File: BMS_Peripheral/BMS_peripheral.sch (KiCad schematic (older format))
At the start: 187 parts, among them J1 isoSPI-Cutout, J2 isoSPI-Cutout, J3 MM_F_VT_16, J4 MM_F_VT_20, Q10 BSS308PE, Q11 NSS1C201MZ4, Q2 BSS308PE, Q3 BSS308PE, Q4 BSS308PE, Q5 BSS308PE, Q7 BSS308PE, Q8 BSS308PE, Q9 BSS308PE, T1 T_LAN_7490100111A, U1 LTC6811-1, U2 24AA01, U3 MCP6001T-I-LT, U4 MCP6001T-I-LT, U5 LTC1380IGN, U6 LTC1380IGN, U7 LTC1380IGN

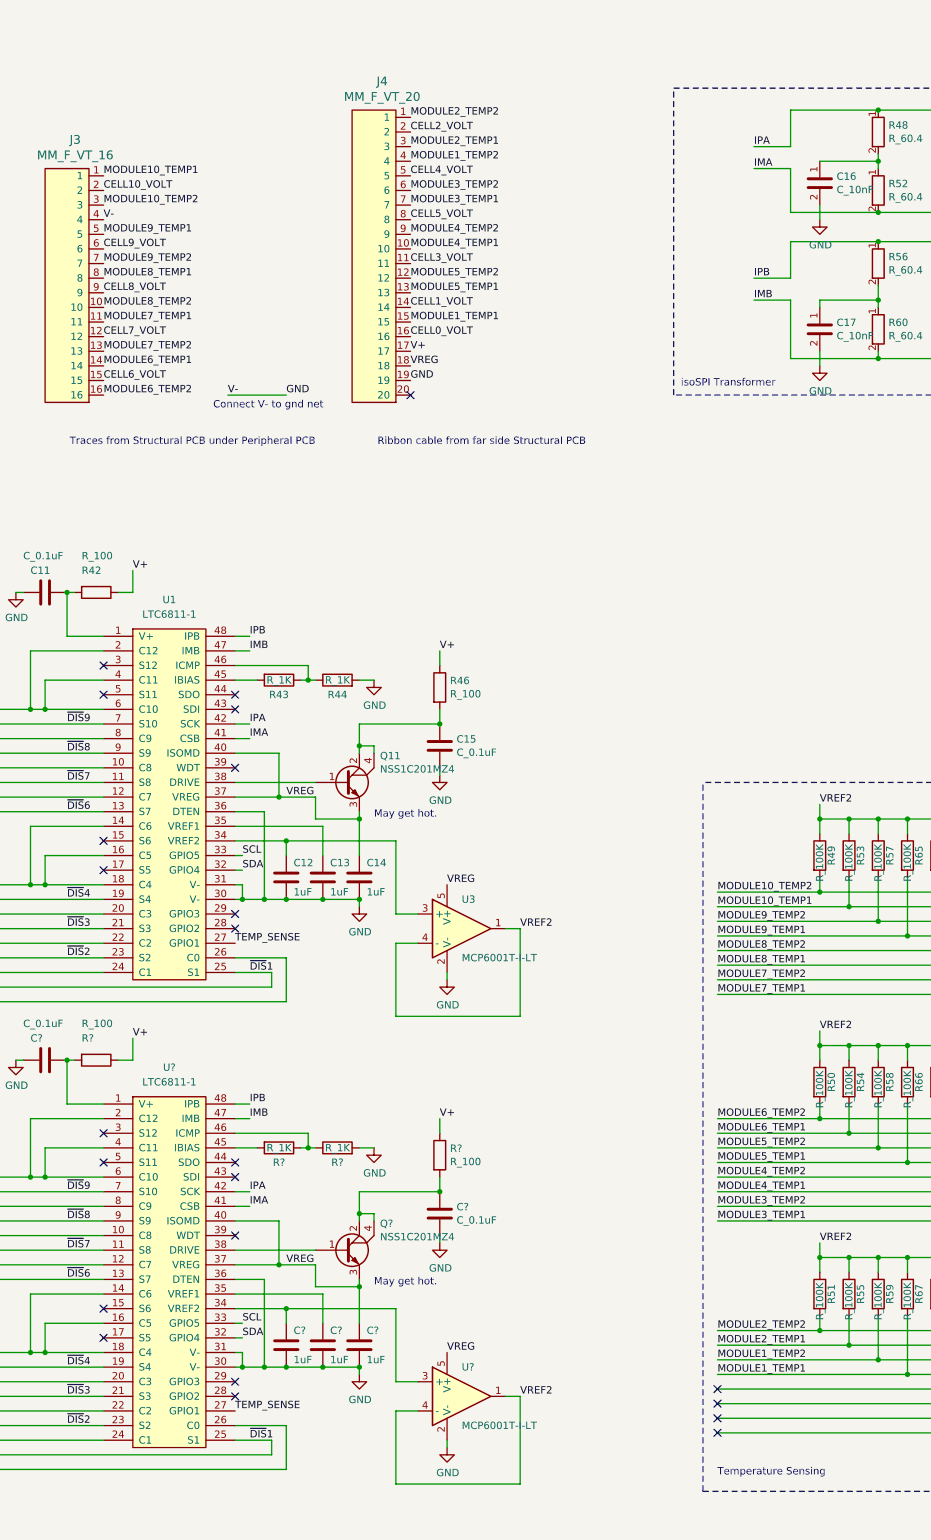
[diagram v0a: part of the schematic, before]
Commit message: Updated muxes for temp sensing
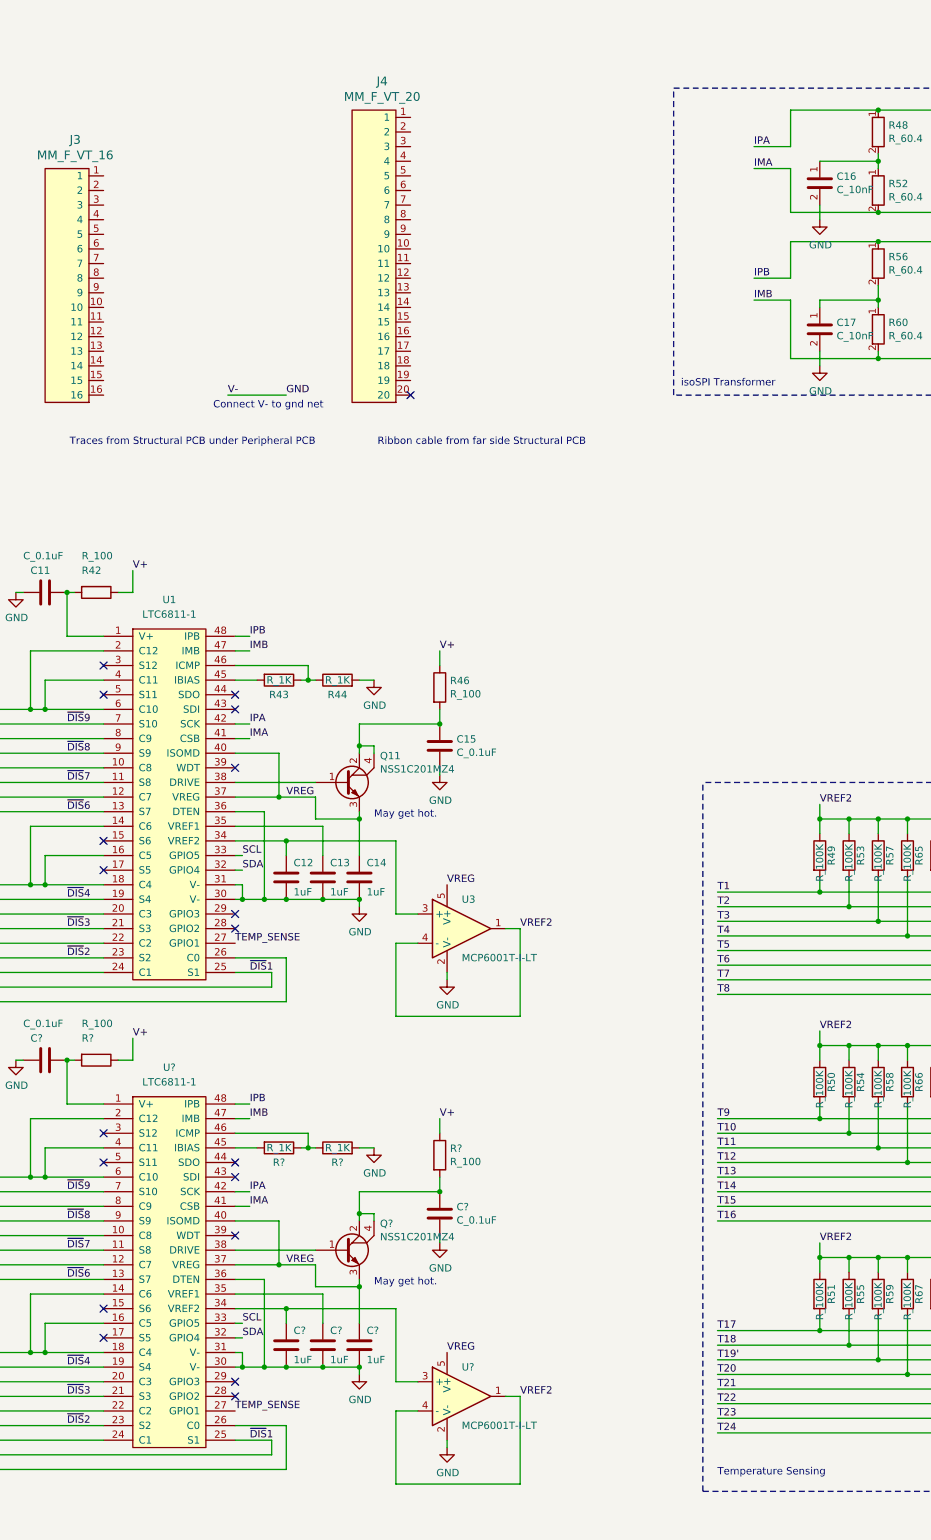
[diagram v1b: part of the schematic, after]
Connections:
- net CELL0_VOLT: no longer J4.16
- net CELL10_VOLT: no longer J3.2
- net CELL1_VOLT: no longer J4.14
- net CELL2_VOLT: no longer J4.2
- net CELL4_VOLT: no longer J4.5
- net CELL5_VOLT: no longer J4.8
- net CELL7_VOLT: no longer J3.12
- net CELL8_VOLT: no longer J3.9
- net CELL9_VOLT: no longer J3.6
- net GND: no longer J3.4, J4.19
- net V+: no longer J4.17
- net VREG: no longer J4.18
- net T21: now reaches R71.2, U7.5 (S4)
- net T22: now reaches R75.2, U7.6 (S5)
- net T23: now reaches R78.2, U7.7 (S6)
- net T24: now reaches R81.2, U7.8 (S7)
- net CELL3_VOLT: no longer names the net of J4.11
- net CELL6_VOLT: no longer names the net of J3.15
- net MODULE10_TEMP1 renamed T2
- net T2: no longer J3.1
- net MODULE10_TEMP2 renamed T1
- net T1: no longer J3.3
- net MODULE1_TEMP1 renamed T20
- net T20: no longer J4.15
- net MODULE1_TEMP2 renamed T19'
- net T19': no longer J4.4
- net MODULE2_TEMP1 renamed T18
- net T18: no longer J4.3
- net MODULE2_TEMP2 renamed T17
- net T17: no longer J4.1
- net MODULE3_TEMP1 renamed T16
- net T16: no longer J4.7
- net MODULE3_TEMP2 renamed T15
- net T15: no longer J4.6
- net MODULE4_TEMP1 renamed T14
- net T14: no longer J4.10
- net MODULE4_TEMP2 renamed T13
- net T13: no longer J4.9
- net MODULE5_TEMP1 renamed T12
- net T12: no longer J4.13
- net MODULE5_TEMP2 renamed T11
- net T11: no longer J4.12
- net MODULE6_TEMP1 renamed T10
- net T10: no longer J3.14
- net MODULE6_TEMP2 renamed T9
- net T9: no longer J3.16
- net MODULE7_TEMP1 renamed T8
- net T8: no longer J3.11
- net MODULE7_TEMP2 renamed T7
- net T7: no longer J3.13
- net MODULE8_TEMP1 renamed T6
- net T6: no longer J3.8
- net MODULE8_TEMP2 renamed T5
- net T5: no longer J3.10
- net MODULE9_TEMP1 renamed T4
- net T4: no longer J3.5
- net MODULE9_TEMP2 renamed T3
- net T3: no longer J3.7
- no-connect marks 41 -> 37
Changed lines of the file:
@@
 	11550 7500 13650 7500
 Text Label 11550 6900 0    50   ~ 0
-MODULE10_TEMP1
+T2
 Text Label 11550 7000 0    50   ~ 0
-MODULE9_TEMP2
+T3
 Text Label 11550 7100 0    50   ~ 0
-MODULE9_TEMP1
+T4
 Text Label 11550 7200 0    50   ~ 0
-MODULE8_TEMP2
+T5
 Text Label 11550 7300 0    50   ~ 0
-MODULE8_TEMP1
+T6
 Text Label 11550 7400 0    50   ~ 0
-MODULE7_TEMP2
+T7
 Text Label 11550 7500 0    50   ~ 0
-MODULE7_TEMP1
+T8
 Wire Wire Line
 	12250 6700 12250 6800
@@
 	11550 9050 13650 9050
 Text Label 11550 8450 0    50   ~ 0
-MODULE6_TEMP1
+T10
 Text Label 11550 8550 0    50   ~ 0
-MODULE5_TEMP2
+T11
 Text Label 11550 8650 0    50   ~ 0
-MODULE5_TEMP1
+T12
 Text Label 11550 8850 0    50   ~ 0
-MODULE4_TEMP1
+T14
 Text Label 11550 8950 0    50   ~ 0
-MODULE3_TEMP2
+T15
 Text Label 11550 9050 0    50   ~ 0
-MODULE3_TEMP1
+T16
 Wire Wire Line
 	12250 8250 12250 8350
@@
 	11550 10500 13650 10500
 Text Label 11550 9800 0    50   ~ 0
-MODULE2_TEMP2
+T17
 Text Label 11550 9900 0    50   ~ 0
-MODULE2_TEMP1
+T18
 Text Label 11550 10000 0    50   ~ 0
-MODULE1_TEMP2
+T19'
 Text Label 11550 10100 0    50   ~ 0
-MODULE1_TEMP1
+T20
 Wire Wire Line
 	12250 9700 12250 9800
@@
 A0 = 0, A1 = 0  Address 0x94
 Text Label 11550 6800 0    50   ~ 0
-MODULE10_TEMP2
+T1
 Text Label 11550 8350 0    50   ~ 0
-MODULE6_TEMP2
+T9
 Text Label 11550 8750 0    50   ~ 0
-MODULE4_TEMP2
+T13
 Wire Wire Line
 	15050 10100 15050 10300
@@
 Wire Wire Line
 	8800 6050 8250 6050
-Text Label 7350 2000 0    50   ~ 0
-CELL10_VOLT
-Text Label 7350 2400 0    50   ~ 0
-CELL9_VOLT
-Text Label 7350 2700 0    50   ~ 0
-CELL8_VOLT
-Text Label 7350 3000 0    50   ~ 0
-CELL7_VOLT
-Text Label 7350 3300 0    50   ~ 0
-CELL6_VOLT
 Wire Notes Line
 	11450 10900 17550 10900
-NoConn ~ 11550 10300
-NoConn ~ 11550 10400
-NoConn ~ 11550 10500
 Wire Notes Line
 	17550 6050 17550 10900
@@
 	1    0    0    -1
 $EndComp
-Text Label 7350 1900 0    50   ~ 0
-MODULE10_TEMP1
-Text Label 7350 2100 0    50   ~ 0
-MODULE10_TEMP2
-Text Label 7350 2300 0    50   ~ 0
-MODULE9_TEMP1
-Text Label 7350 2500 0    50   ~ 0
-MODULE9_TEMP2
-Text Label 7350 2600 0    50   ~ 0
-MODULE8_TEMP1
-Text Label 7350 2800 0    50   ~ 0
-MODULE8_TEMP2
-Text Label 7350 2900 0    50   ~ 0
-MODULE7_TEMP1
-Text Label 7350 3100 0    50   ~ 0
-MODULE7_TEMP2
-Text Label 7350 3200 0    50   ~ 0
-MODULE6_TEMP1
-Text Label 7350 3400 0    50   ~ 0
-MODULE6_TEMP2
-Text Label 7350 2200 0    50   ~ 0
-V-
-Text Label 9450 2200 0    50   ~ 0
-CELL5_VOLT
-Text Label 9450 1900 0    50   ~ 0
-CELL4_VOLT
-Text Label 9450 2500 0    50   ~ 0
-CELL3_VOLT
-Text Label 9450 1600 0    50   ~ 0
-CELL2_VOLT
-Text Label 9450 2700 0    50   ~ 0
-MODULE5_TEMP1
-Text Label 9450 2600 0    50   ~ 0
-MODULE5_TEMP2
-Text Label 9450 2400 0    50   ~ 0
-MODULE4_TEMP1
-Text Label 9450 2300 0    50   ~ 0
-MODULE4_TEMP2
-Text Label 9450 2100 0    50   ~ 0
-MODULE3_TEMP1
-Text Label 9450 2000 0    50   ~ 0
-MODULE3_TEMP2
-Text Label 9450 1700 0    50   ~ 0
-MODULE2_TEMP1
-Text Label 9450 1500 0    50   ~ 0
-MODULE2_TEMP2
-Text Label 9450 2900 0    50   ~ 0
-MODULE1_TEMP1
-Text Label 9450 1800 0    50   ~ 0
-MODULE1_TEMP2
-Text Label 9450 3100 0    50   ~ 0
-V+
-Text Label 9450 2800 0    50   ~ 0
-CELL1_VOLT
-Text Label 9450 3000 0    50   ~ 0
-CELL0_VOLT
 Text Label 1750 750  2    50   ~ 0
 CELL16_VOLT
@@
 	1    0    0    -1
 $EndComp
-Text Label 9450 3300 0    50   ~ 0
-GND
 NoConn ~ 9450 3400
 Wire Wire Line
@@
 Wire Wire Line
 	1750 7550 2600 7550
-NoConn ~ 11550 10200
-Text Label 9450 3200 0    50   ~ 0
-VREG
 $Comp
 L formula:T_LAN_7490100111A T1
@@
 Wire Wire Line
 	6000 10750 6000 15550
+Text Label 11550 10200 0    50   ~ 0
+T21
+Text Label 11550 10300 0    50   ~ 0
+T22
+Text Label 11550 10400 0    50   ~ 0
+T23
+Text Label 11550 10500 0    50   ~ 0
+T24
 $EndSCHEMATC
